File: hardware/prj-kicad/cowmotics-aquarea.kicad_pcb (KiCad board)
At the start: 4 copper layers, 80 x 50 mm, 27 parts, among them J1 CONN_RJ45, Q1 BC846, T1 TRANSFORMER_1_1, U1 KSZ8091RN, X1 50MHz

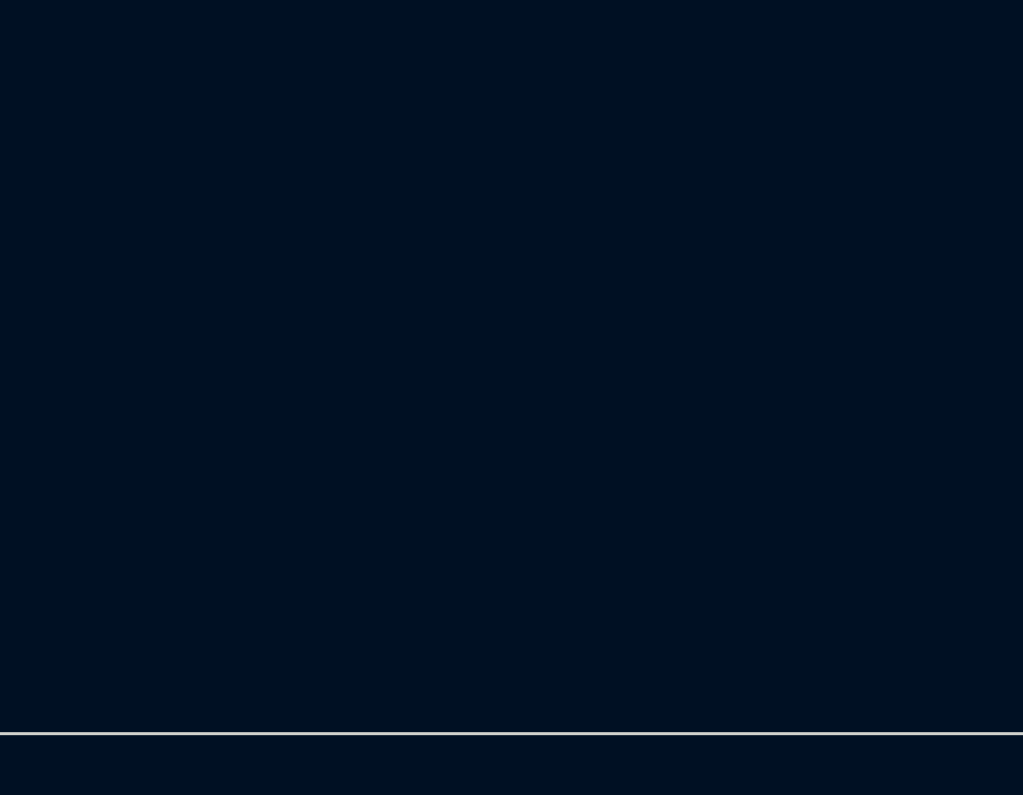
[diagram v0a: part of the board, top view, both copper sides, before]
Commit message: = ADD: Insert ESP32 processor and his main components
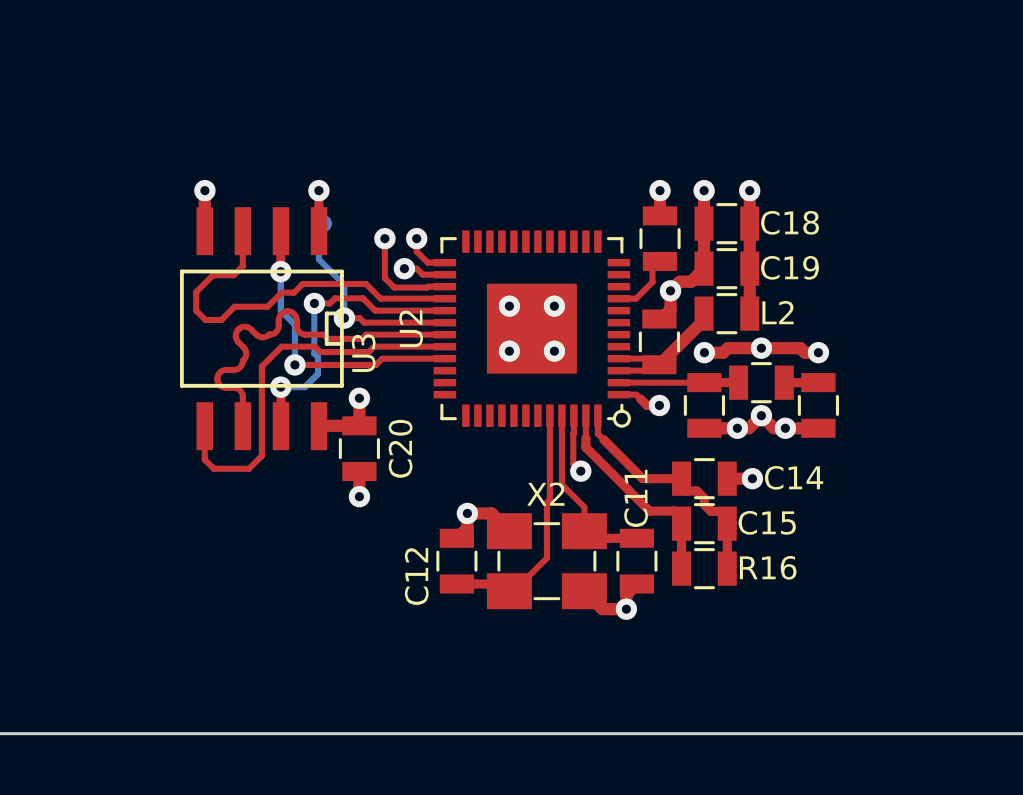
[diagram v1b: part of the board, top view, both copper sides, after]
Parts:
- added C11: 10pF, cowmotics-aquarea:SMD0603, F.Cu at (172.0, 124.2)
- added C12: 10pF, cowmotics-aquarea:SMD0603, F.Cu at (166.0, 124.2)
- added C13: 10nF, cowmotics-aquarea:SMD0603, F.Cu at (172.8, 116.9)
- added C14: 10nF, cowmotics-aquarea:SMD0603, F.Cu at (174.2, 121.5)
- added C15: 3,3nF, cowmotics-aquarea:SMD0603, F.Cu at (174.2, 123.0)
- added C16: C, cowmotics-aquarea:SMD0603, F.Cu at (174.2, 119.1)
- added C17: C, cowmotics-aquarea:SMD0603, F.Cu at (178.1, 119.1)
- added C18: 1uF, cowmotics-aquarea:SMD0603, F.Cu at (175.0, 113.0)
- added C19: 100nF, cowmotics-aquarea:SMD0603, F.Cu at (175.0, 114.5)
- added C20: 100nF, cowmotics-aquarea:SMD0603, F.Cu at (162.8, 120.5)
- added L2: FB100, cowmotics-aquarea:SMD0603, F.Cu at (175.0, 116.0)
- added L3: INDUCTOR, cowmotics-aquarea:SMD0603, F.Cu at (176.2, 118.3)
- added R15: 10k, cowmotics-aquarea:SMD0603, F.Cu at (172.8, 113.5)
- added R16: 20k, cowmotics-aquarea:SMD0603, F.Cu at (174.2, 124.5)
- added U2: ESP32, cowmotics-aquarea:QFN48-04, F.Cu at (168.5, 116.5)
- added U3: SST25VF016, cowmotics-aquarea:SOIC-8, F.Cu at (159.5, 116.5)
- added X2: 40MHz, cowmotics-aquarea:Q_3.2x2.5, F.Cu at (169.0, 124.2)
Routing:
- net GND: track 185.9 -> 269.1 mm, vias 43 -> 60
- net +3.3V: track 81.3 -> 106.0 mm, vias 8 -> 12
- net FL_D0: track 0.00 -> 12.8 mm
- net FL_D2: track 0.00 -> 12.8 mm
- net FL_SCK: track 0.00 -> 12.7 mm
- net FL_D1: track 0.00 -> 9.74 mm, vias 0 -> 2
- net FL_D3: track 0.00 -> 9.72 mm, vias 0 -> 2
- net FL_SCS: track 0.00 -> 9.71 mm, vias 0 -> 2
- net +VMEM: track 0.00 -> 8.64 mm, vias 0 -> 2
- net Net-(C12-Pad1): track 0.00 -> 8.35 mm
- net Net-(C14-Pad1): track 0.00 -> 8.01 mm
- net Net-(C15-Pad1): track 0.00 -> 6.91 mm
- net Net-(C11-Pad1): track 0.00 -> 6.01 mm
- net Net-(C13-Pad1): track 0.00 -> 5.18 mm
- net Net-(C16-Pad1): track 0.00 -> 3.99 mm
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
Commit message: = UPD: Finish ESP32 routing (eth, boot, console, ...)
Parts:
- added A1: ANTENNA, cowmotics-aquarea:CONN_SMA_RA, F.Cu at (183.5, 118.5)
- added C21: 100nF, cowmotics-aquarea:SMD0603, F.Cu at (164.2, 119.5)
- added C22: 1uF, cowmotics-aquarea:SMD0603, F.Cu at (172.8, 110.8)
- added C23: 1uF, cowmotics-aquarea:SMD0603, F.Cu at (183.5, 110.0)
- added R13: 10k, cowmotics-aquarea:SMD0603, F.Cu at (149.0, 118.8)
- added R17: 49.9, cowmotics-aquarea:SMD0603, F.Cu at (149.0, 120.5)
- added R18: 0, cowmotics-aquarea:SMD0603, F.Cu at (146.8, 115.0)
- added R19: 10k, cowmotics-aquarea:SMD0603, F.Cu at (166.5, 111.0)
- added SW1: SW_PUSH, cowmotics-aquarea:SW_PTS840, F.Cu at (187.0, 110.0)
- added SW2: SW_PUSH, cowmotics-aquarea:SW_434123043816, F.Cu at (152.0, 122.5)
- added TP10: CONN_1, cowmotics-aquarea:TP_SMD, B.Cu at (169.5, 113.0)
- added TP11: CONN_1, cowmotics-aquarea:TP_SMD, B.Cu at (171.0, 114.0)
- added TP12: CONN_1, cowmotics-aquarea:TP_SMD, B.Cu at (171.0, 109.5)
- added TP3: CONN_1, cowmotics-aquarea:TP_SMD, F.Cu at (158.0, 125.2)
- added TP4: CONN_1, cowmotics-aquarea:TP_SMD, F.Cu at (160.5, 125.2)
- added TP5: CONN_1, cowmotics-aquarea:TP_SMD, B.Cu at (146.0, 121.2)
- added TP6: CONN_1, cowmotics-aquarea:TP_SMD, B.Cu at (143.5, 121.2)
- added TP7: CONN_1, cowmotics-aquarea:TP_SMD, F.Cu at (163.0, 125.2)
- added TP8: CONN_1, cowmotics-aquarea:TP_SMD, B.Cu at (167.7, 113.5)
- added TP9: CONN_1, cowmotics-aquarea:TP_SMD, B.Cu at (169.5, 109.5)
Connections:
- T1 pad 12: (no net) -> unconnected-(T1-Pad12)
- T1 pad 13: (no net) -> unconnected-(T1-Pad13)
- T1 pad 4: (no net) -> unconnected-(T1-Pad4)
- T1 pad 5: (no net) -> unconnected-(T1-Pad5)
- U2 pad 17: unconnected-(U2-Pad17) -> Net-(TP11-Pad1)
- U2 pad 18: unconnected-(U2-Pad18) -> Net-(TP10-Pad1)
- U2 pad 20: ETH_RXER -> Net-(R18-Pad2)
- U2 pad 21: unconnected-(U2-Pad21) -> Net-(TP8-Pad1)
- U2 pad 22: unconnected-(U2-Pad22) -> BOOT2
- U2 pad 23: CLK_50M -> BOOT0
- U2 pad 24: unconnected-(U2-Pad24) -> ETH_IRQ
- U2 pad 34: unconnected-(U2-Pad34) -> ETH_MDC
- U2 pad 35: unconnected-(U2-Pad35) -> CLK50_EN
- U2 pad 36: unconnected-(U2-Pad36) -> ETH_MDIO
- U2 pad 40: unconnected-(U2-Pad40) -> U0_RX
- U2 pad 41: unconnected-(U2-Pad41) -> U0_TX
- U2 pad 6: unconnected-(U2-Pad6) -> RJ45_LED
- U2 pad 8: unconnected-(U2-Pad8) -> BUTTON
- X1 pad 1: CLK_EN -> CLK50_EN
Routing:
- net GND: track 269.1 -> 395.0 mm, vias 60 -> 97
- net RJ45_LED: track 0.89 -> 40.8 mm, vias 1 -> 2
- net BOOT0: track 0.00 -> 37.9 mm, vias 0 -> 2
- net +3.3V: track 106.0 -> 143.2 mm, vias 12 -> 15
- net Net-(R18-Pad2): track 0.00 -> 35.7 mm, vias 0 -> 2
- net ETH_IRQ: track 1.77 -> 36.9 mm, vias 1 -> 2
- net ETH_RXD0: track 1.96 -> 36.9 mm, vias 1 -> 2
- net ETH_RXD1: track 2.06 -> 36.9 mm, vias 1 -> 2
- net ETH_TXEN: track 2.19 -> 37.0 mm, vias 1 -> 2
- net ETH_CRSDV: track 2.66 -> 36.7 mm, vias 1 -> 2
- net ETH_TXD0: track 3.56 -> 36.9 mm, vias 1 -> 2
- net ETH_TXD1: track 3.68 -> 36.9 mm, vias 1 -> 2
- net CLK50_EN: track 0.00 -> 29.0 mm, vias 0 -> 2
- net ETH_MDIO: track 3.78 -> 32.3 mm, vias 1 -> 2
- net ETH_MDC: track 3.60 -> 31.1 mm, vias 1 -> 2
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
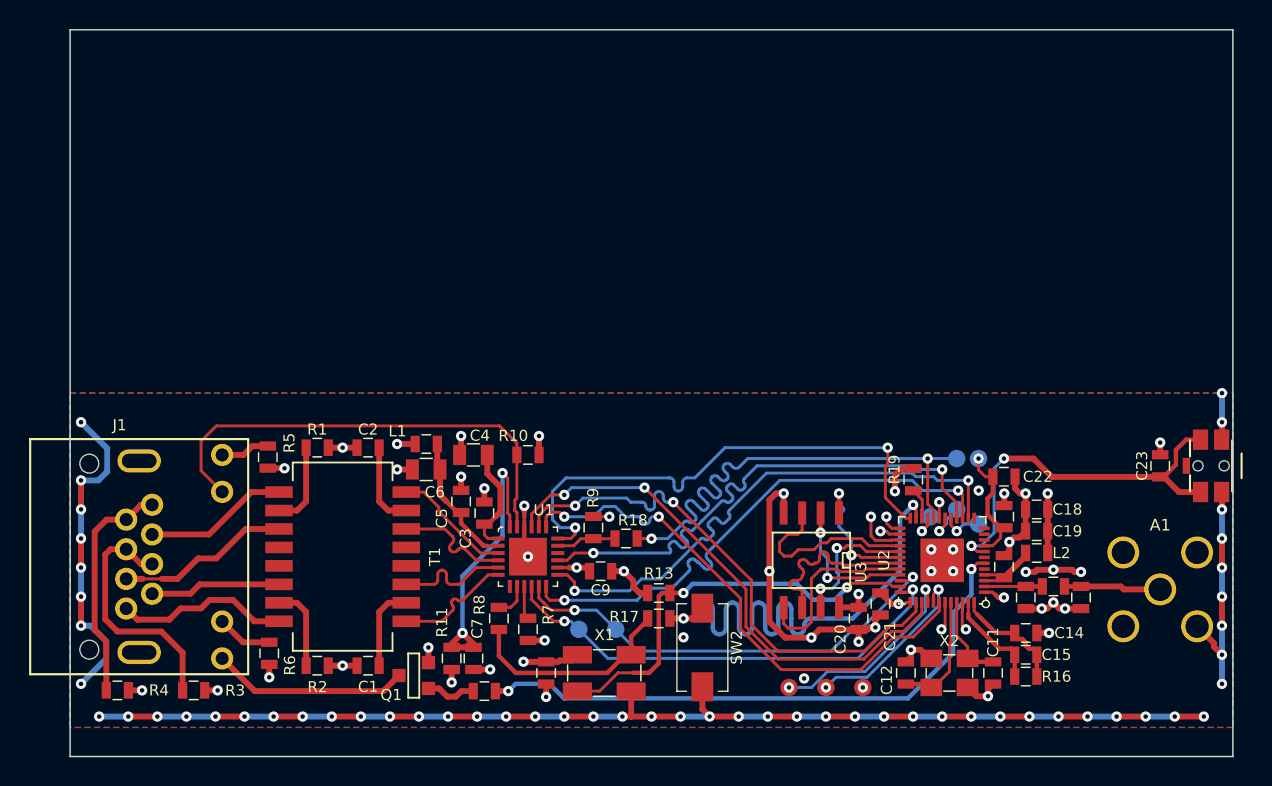
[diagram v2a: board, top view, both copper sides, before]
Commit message: = ADD: Insert Aquarea serial interface and power supply
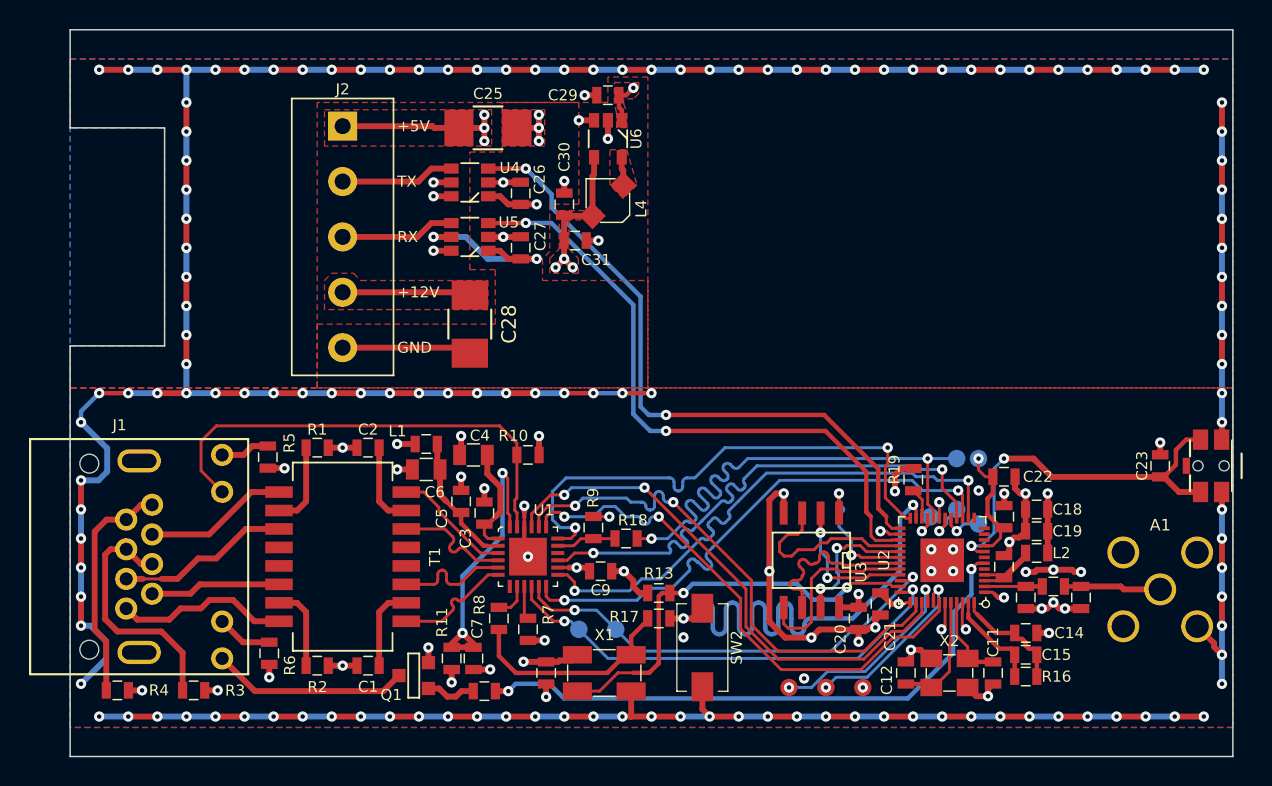
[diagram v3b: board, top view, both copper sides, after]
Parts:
- added C25: 10uF, cowmotics-aquarea:SMD1210, F.Cu at (137.2, 86.8)
- added C26: 100nF, cowmotics-aquarea:SMD0603, F.Cu at (139.5, 91.2)
- added C27: 100nF, cowmotics-aquarea:SMD0603, F.Cu at (139.5, 95.0)
- added C28: 10uF, cowmotics-aquarea:SMD1210, F.Cu at (136.0, 100.2)
- added C29: 470pF, cowmotics-aquarea:SMD0603, F.Cu at (145.5, 84.5)
- added C30: 4,7uF, cowmotics-aquarea:SMD0603, F.Cu at (142.5, 92.0)
- added C31: 4,7uF, cowmotics-aquarea:SMD0603, F.Cu at (143.2, 94.5)
- added J2: CONN_5, cowmotics-aquarea:CONN_691243310005, F.Cu at (127.2, 86.6)
- added L4: 2,2uH, cowmotics-aquarea:I_CDRH2D14, F.Cu at (145.5, 91.8)
- added U4: SN74LVC1T45, cowmotics-aquarea:SOT23-6, F.Cu at (136.0, 90.5)
- added U5: SN74LVC1T45, cowmotics-aquarea:SOT23-6, F.Cu at (136.0, 94.2)
- added U6: LM3671, cowmotics-aquarea:SOT23-5, F.Cu at (145.5, 87.5)
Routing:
- net GND: track 395.0 -> 616.1 mm, vias 97 -> 186
- net +3.3V: track 143.2 -> 204.4 mm, vias 15 -> 21
- net U2_RXD: track 1.52 -> 45.4 mm, vias 1 -> 2
- net +5V: track 0.00 -> 42.4 mm, vias 0 -> 7
- net U2_TXD: track 3.46 -> 44.2 mm, vias 1 -> 2
- net +12V: track 0.00 -> 8.83 mm
- net /Aquarea Interface/AQ_RX: track 0.00 -> 7.87 mm
- net /Aquarea Interface/AQ_TX: track 0.00 -> 7.85 mm
- net /Aquarea Interface/U6_SW: track 0.00 -> 1.96 mm
- added copper zone on F.Cu, net +12V
- added copper zone on In2.Cu, net +12V
- added copper zone on F.Cu, net +3.3V
- added copper zone on F.Cu, net +5V
- added copper zone on In2.Cu, net +5V
- added copper zone on F.Cu, net /Aquarea Interface/U6_SW
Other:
- outline, holes or cut-outs redrawn
- board text added: "+12V"
- board text added: "+5V"
- board text added: "GND"
- board text added: "RX"
- board text added: "TX"

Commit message: = ADD: Create production files for rev1
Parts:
- added agilack-11.5: 450px, cowmotics-aquarea:logo-agilack-11.5, F.Cu at (155.0, 109.8)
- added ohw_logo: VAL**, cowmotics-aquarea:logo-ohw, F.Cu at (143.5, 101.0)
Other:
- board text added: "Agilack CC-by-SA"
- board text added: "cowmotics-aquarea"
- board text added: "rev1"
